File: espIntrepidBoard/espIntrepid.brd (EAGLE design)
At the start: 64 x 56 mm, 23 parts, among them Q1 TRANS_NPN, Q7 TRANS_NPN, U1 ESP32DEV_38, U2 MOSFET_P, U3 LTV-847, U5 SN65HVD232DSOIC8, U6 LTV-817

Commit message: Finished board
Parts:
- moved R1 0.50 mm to (56.0, 47.5)
- moved JP7 0.10 mm to (61.0, 3.40)
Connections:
- net N$7: now also JP1.6; no longer JP1.7
- net N$8: now also JP1.7; no longer JP1.6
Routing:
- net N$8: track 35.6 -> 29.7 mm, vias 2 -> 0
- net N$7: track 28.6 -> 26.4 mm
- net +12V: track 79.1 -> 79.9 mm
- net ABS_UC: track 7.32 -> 6.72 mm
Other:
- outline, holes or cut-outs redrawn
- board text added: "ESP32_Dashboard V 1.0 2/16/25"
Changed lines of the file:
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@@
 <board>
 <plain>
-<wire x1="0" y1="0" x2="64" y2="0" width="0" layer="20"/>
-<wire x1="64" y1="0" x2="64" y2="56" width="0" layer="20"/>
-<wire x1="64" y1="56" x2="0" y2="56" width="0" layer="20"/>
-<wire x1="0" y1="56" x2="0" y2="0" width="0" layer="20"/>
 <hole x="3.5" y="3.5" drill="2.5"/>
 <hole x="3.5" y="52.5" drill="2.5"/>
 <hole x="55" y="3.5" drill="2.5"/>
 <hole x="55" y="52.5" drill="2.5"/>
+<wire x1="3" y1="0" x2="61" y2="0" width="0" layer="20"/>
+<wire x1="64" y1="3" x2="64" y2="53" width="0" layer="20"/>
+<wire x1="61" y1="56" x2="3" y2="56" width="0" layer="20"/>
+<wire x1="0" y1="53" x2="0" y2="3" width="0" layer="20"/>
+<wire x1="0" y1="53" x2="3" y2="56" width="0" layer="20" curve="-90"/>
+<wire x1="61" y1="56" x2="64" y2="53" width="0" layer="20" curve="-90"/>
+<wire x1="64" y1="3" x2="61" y2="0" width="0" layer="20" curve="-90"/>
+<wire x1="3" y1="0" x2="0" y2="3" width="0" layer="20" curve="-90"/>
+<text x="14.5" y="51" size="1.27" layer="25">ESP32_Dashboard
+V 1.0      2/16/25</text>
 </plain>
 <attributes>
@@
 <attribute name="NAME" x="50.2" y="48.6" size="0.6096" layer="25" rot="R270"/>
 </element>
-<element name="R1" library="DR" package="M1206" value="" x="56" y="48" smashed="yes">
-<attribute name="NAME" x="58.73" y="47.27" size="1.27" layer="25"/>
-<attribute name="VALUE" x="54.73" y="45.46" size="1.27" layer="27"/>
+<element name="R1" library="DR" package="M1206" value="" x="56" y="47.5" smashed="yes">
+<attribute name="NAME" x="58.73" y="46.77" size="1.27" layer="25"/>
+<attribute name="VALUE" x="54.73" y="44.96" size="1.27" layer="27"/>
 </element>
 <element name="Q1" library="DR" package="SOT-23" value="TRANS_NPN" x="47" y="47" smashed="yes" rot="R270">
@@
 <attribute name="NAME" x="45.7" y="21.6" size="1.778" layer="25"/>
 </element>
-<element name="JP7" library="pinhead" library_urn="urn:adsk.eagle:library:325" package="1X02" package3d_urn="urn:adsk.eagle:package:22435/2" value="" x="61" y="3.3" smashed="yes" rot="R270">
-<attribute name="NAME" x="62.8288" y="5.9162" size="1.27" layer="25" ratio="10" rot="R270"/>
-<attribute name="POPULARITY" value="98" x="61" y="3.3" size="1.778" layer="27" rot="R270" display="off"/>
-<attribute name="VALUE" x="57.825" y="5.84" size="1.27" layer="27" rot="R270"/>
+<element name="JP7" library="pinhead" library_urn="urn:adsk.eagle:library:325" package="1X02" package3d_urn="urn:adsk.eagle:package:22435/2" value="" x="61" y="3.4" smashed="yes" rot="R270">
+<attribute name="NAME" x="62.8288" y="6.0162" size="1.27" layer="25" ratio="10" rot="R270"/>
+<attribute name="POPULARITY" value="98" x="61" y="3.4" size="1.778" layer="27" rot="R270" display="off"/>
+<attribute name="VALUE" x="57.825" y="5.94" size="1.27" layer="27" rot="R270"/>
 </element>
 </elements>
@@
 <vertex x="39" y="56.5"/>
 <vertex x="65.5" y="56.5"/>
-<vertex x="65.5" y="0"/>
-<vertex x="-0.5" y="0"/>
+<vertex x="65.5" y="-1"/>
+<vertex x="-0.5" y="-1"/>
 </polygon>
 <contactref element="JP2" pad="3"/>
@@
 <vertex x="-0.5" y="41.5"/>
 <vertex x="39" y="41.5"/>
-<vertex x="39" y="56"/>
-<vertex x="64.5" y="56"/>
+<vertex x="39" y="57"/>
+<vertex x="64.5" y="57"/>
 <vertex x="64.5" y="-0.5"/>
 </polygon>
@@
 <contactref element="U3" pad="16"/>
 <contactref element="U3" pad="14"/>
-<wire x1="55" y1="36.92" x2="53" y2="36.92" width="0.508" layer="1"/>
-<wire x1="53" y1="36.92" x2="52.58" y2="36.92" width="0.508" layer="1"/>
-<wire x1="52.58" y1="36.92" x2="51.5" y2="38" width="0.508" layer="1"/>
-<wire x1="51.5" y1="38" x2="51.5" y2="41" width="0.508" layer="1"/>
-<wire x1="51.5" y1="41" x2="52.5" y2="42" width="0.508" layer="1"/>
+<wire x1="55" y1="36.92" x2="53" y2="36.92" width="0.8128" layer="1"/>
+<wire x1="53" y1="36.92" x2="52.58" y2="36.92" width="0.8128" layer="1"/>
+<wire x1="52.58" y1="36.92" x2="51.5" y2="38" width="0.8128" layer="1"/>
+<wire x1="51.5" y1="38" x2="51.5" y2="41" width="0.8128" layer="1"/>
+<wire x1="51.5" y1="41" x2="52.5" y2="42" width="0.8128" layer="1"/>
 <wire x1="52.5" y1="42" x2="55" y2="42" width="0.508" layer="1"/>
-<wire x1="42.46" y1="52.9" x2="42.5" y2="52.86" width="0.508" layer="1"/>
-<wire x1="53.54381875" y1="49.95" x2="53.56381875" y2="49.95" width="0.508" layer="1"/>
-<wire x1="53.56381875" y1="49.95" x2="56" y2="49.95" width="0.508" layer="1"/>
-<wire x1="42.46" y1="52.9" x2="45.38" y2="49.95" width="0.508" layer="1"/>
-<wire x1="45.38" y1="49.95" x2="53.54381875" y2="49.95" width="0.508" layer="1"/>
-<wire x1="56" y1="49.95" x2="57.4" y2="48.6" width="0.508" layer="1"/>
-<wire x1="57.4" y1="48.6" x2="57.4" y2="48" width="0.508" layer="1"/>
-<wire x1="57.4" y1="48" x2="57.4" y2="44.4" width="0.508" layer="1"/>
-<wire x1="57.4" y1="44.4" x2="55" y2="42" width="0.508" layer="1"/>
-<wire x1="55" y1="42" x2="53.45" y2="42" width="0.4064" layer="1"/>
+<wire x1="44.374915625" y1="49.45" x2="42.46" y2="51.3845875" width="0.8128" layer="1"/>
+<wire x1="42.46" y1="52.9" x2="42.46" y2="51.3845875" width="0.8128" layer="1"/>
+<wire x1="44.374915625" y1="49.45" x2="56.51851875" y2="49.45" width="0.8128" layer="1"/>
+<wire x1="56.51851875" y1="49.45" x2="57.4" y2="48.6" width="0.8128" layer="1"/>
+<wire x1="57.4" y1="48.6" x2="57.4" y2="47.5" width="0.508" layer="1"/>
+<wire x1="57.4" y1="47.5" x2="57.4" y2="44.4" width="0.8128" layer="1"/>
+<wire x1="57.4" y1="44.4" x2="55" y2="42" width="0.8128" layer="1"/>
+<wire x1="55" y1="42" x2="53.45" y2="42" width="0.8128" layer="1"/>
 <wire x1="53.45" y1="42" x2="49.4" y2="46.05" width="0.4064" layer="1"/>
 <contactref element="JP7" pad="1"/>
-<wire x1="61" y1="4.57" x2="59.93" y2="4.57" width="0.8128" layer="16"/>
+<wire x1="61" y1="4.67" x2="59.93" y2="4.57" width="0.8128" layer="16"/>
 <wire x1="53.5" y1="11" x2="53.5" y2="36.5" width="0.8128" layer="16"/>
 <wire x1="53.5" y1="36.5" x2="53" y2="36.5" width="0.8128" layer="16"/>
@@
 <wire x1="47.1" y1="47" x2="48.05" y2="47.95" width="0.508" layer="1"/>
 <wire x1="48.05" y1="47.95" x2="49.4" y2="47.95" width="0.508" layer="1"/>
-<wire x1="49.4" y1="47.95" x2="49.95" y2="48.5" width="0.508" layer="1"/>
-<wire x1="49.95" y1="48.5" x2="54.5" y2="48.5" width="0.508" layer="1"/>
-<wire x1="54.5" y1="48.5" x2="54.6" y2="48.4" width="0.508" layer="1"/>
-<wire x1="54.6" y1="48.4" x2="54.6" y2="48" width="0.508" layer="1"/>
+<wire x1="49.4" y1="47.95" x2="49.45" y2="48" width="0.508" layer="1"/>
+<wire x1="49.45" y1="48" x2="54.5" y2="48" width="0.508" layer="1"/>
+<wire x1="54.5" y1="48" x2="54.6" y2="47.9" width="0.508" layer="1"/>
+<wire x1="54.6" y1="47.9" x2="54.6" y2="47.5" width="0.508" layer="1"/>
 </signal>
 <signal name="ABS">
@@
 <signal name="ABS_UC">
 <contactref element="R8" pad="1"/>
-<wire x1="39.68" y1="26.92" x2="40.1" y2="26.5" width="0.4064" layer="1"/>
 <contactref element="U1" pad="30"/>
 <wire x1="34.9" y1="30.18" x2="36.42" y2="30.18" width="0.6096" layer="1"/>
@@
 <signal name="N$7">
 <contactref element="JP1" pad="3"/>
-<contactref element="JP1" pad="7"/>
 <contactref element="U1" pad="15"/>
 <wire x1="9.5" y1="14.94" x2="7.56" y2="14.94" width="0.508" layer="1"/>
@@
 <wire x1="5.34" y1="25.16" x2="3.1" y2="25.16" width="0.508" layer="16"/>
 <wire x1="6" y1="24.5" x2="5.34" y2="25.16" width="0.508" layer="16"/>
-<wire x1="3.1" y1="35.32" x2="5.18" y2="35.32" width="0.508" layer="16"/>
-<wire x1="5.18" y1="35.32" x2="6" y2="34.5" width="0.508" layer="16"/>
-<wire x1="6" y1="34.5" x2="6" y2="24.5" width="0.508" layer="16"/>
+<wire x1="6" y1="32.5" x2="5.68" y2="32.82" width="0.508" layer="16"/>
+<wire x1="6" y1="32.5" x2="6" y2="24.5" width="0.508" layer="16"/>
+<contactref element="JP1" pad="6"/>
+<wire x1="5.68" y1="32.82" x2="3.14" y2="32.82" width="0.4064" layer="16"/>
+<wire x1="3.14" y1="32.82" x2="3.1" y2="32.78" width="0.4064" layer="16"/>
 </signal>
 <signal name="N$8">
-<contactref element="JP1" pad="6"/>
 <contactref element="JP1" pad="2"/>
 <contactref element="U1" pad="12"/>
 <wire x1="9.5" y1="22.56" x2="3.16" y2="22.56" width="0.508" layer="1"/>
 <wire x1="3.16" y1="22.56" x2="3.1" y2="22.62" width="0.508" layer="1"/>
-<wire x1="3.1" y1="32.78" x2="6.78" y2="32.78" width="0.508" layer="1"/>
-<wire x1="6.78" y1="32.78" x2="7" y2="33" width="0.508" layer="1"/>
-<wire x1="7" y1="33" x2="7" y2="36.5" width="0.508" layer="1"/>
-<via x="7" y="36.5" extent="1-16" drill="0.6096"/>
-<via x="11.5" y="36.5" extent="1-16" drill="0.6096"/>
-<wire x1="11.5" y1="36.5" x2="12.5" y2="35.5" width="0.508" layer="1"/>
+<wire x1="11" y1="34" x2="12.5" y2="32.5" width="0.508" layer="1"/>
 <wire x1="12.5" y1="23" x2="12" y2="22.5" width="0.508" layer="1"/>
 <wire x1="12" y1="22.5" x2="9.56" y2="22.5" width="0.508" layer="1"/>
 <wire x1="9.56" y1="22.5" x2="9.5" y2="22.56" width="0.508" layer="1"/>
-<wire x1="7" y1="36.5" x2="11.5" y2="36.5" width="0.254" layer="16"/>
-<wire x1="12.5" y1="35.5" x2="12.5" y2="23" width="0.508" layer="1"/>
+<wire x1="12.5" y1="32.5" x2="12.5" y2="23" width="0.508" layer="1"/>
+<contactref element="JP1" pad="7"/>
+<wire x1="3.1" y1="35.32" x2="6.18" y2="35.32" width="0.4064" layer="1"/>
+<wire x1="6.18" y1="35.32" x2="7.5" y2="34" width="0.4064" layer="1"/>
+<wire x1="7.5" y1="34" x2="11" y2="34" width="0.3048" layer="1"/>
 </signal>
 </signals>
@@
 </drawing>
 <compatibility>
+<note version="6.3" minversion="6.2.2" severity="warning">
+Since Version 6.2.2 text objects can contain more than one line,
+which will not be processed correctly with this version.
+</note>
 <note version="8.2" severity="warning">
 Since Version 8.2, EAGLE supports online libraries. The ids

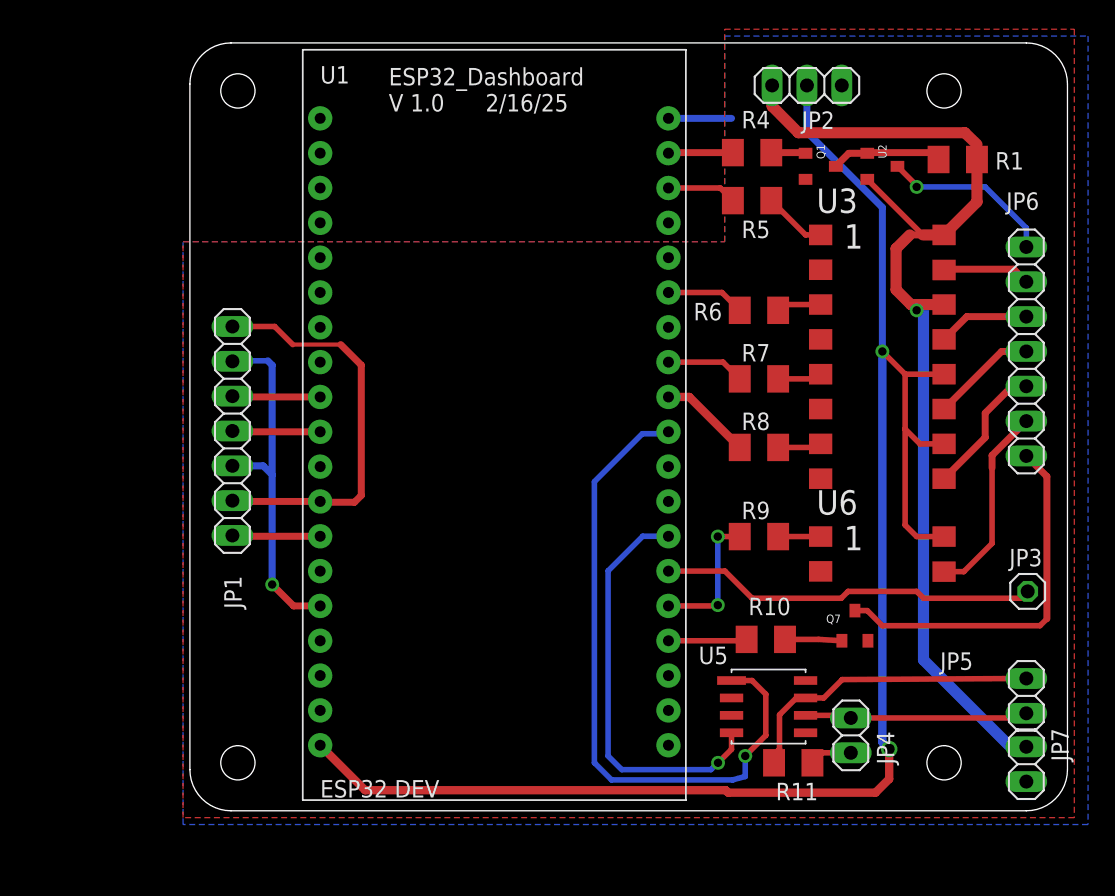
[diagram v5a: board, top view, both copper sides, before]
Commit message: Made fixes to board, started V1.1
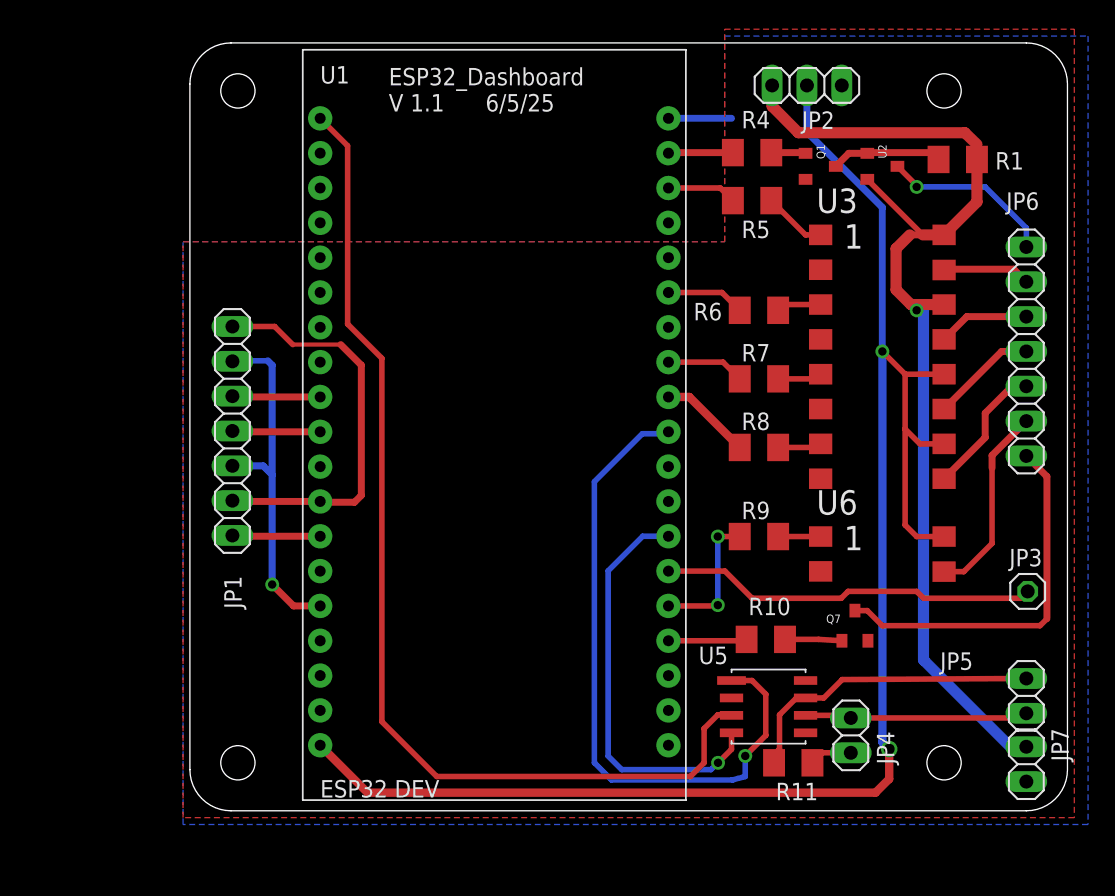
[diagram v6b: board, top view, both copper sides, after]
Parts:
- U5: value SN65HVD232DSOIC8 -> SN65HVD233D
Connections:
- new net 3.3V: U1.1, U5.3
- net GND: now also U5.8
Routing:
- net 3.3V: track 0.00 -> 76.4 mm
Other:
- board text added: "ESP32_Dashboard V 1.1 6/5/25"
- board text removed: "ESP32_Dashboard V 1.0 2/16/25"
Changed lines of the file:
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@@
 <layer number="56" name="wert" color="7" fill="1" visible="no" active="no"/>
 <layer number="57" name="tCAD" color="7" fill="1" visible="no" active="no"/>
+<layer number="88" name="SimResults" color="9" fill="1" visible="no" active="no"/>
+<layer number="89" name="SimProbes" color="9" fill="1" visible="no" active="no"/>
 <layer number="90" name="Modules" color="5" fill="1" visible="no" active="no"/>
 <layer number="91" name="Nets" color="2" fill="1" visible="no" active="no"/>
@@
 <wire x1="3" y1="0" x2="0" y2="3" width="0" layer="20" curve="-90"/>
 <text x="14.5" y="51" size="1.27" layer="25">ESP32_Dashboard
-V 1.0      2/16/25</text>
+V 1.1      6/5/25</text>
 </plain>
 <attributes>
@@
 <attribute name="VALUE" x="40.73" y="9.96" size="1.27" layer="27"/>
 </element>
-<element name="U5" library="DR" package="SOIC-8" value="SN65HVD232DSOIC8" x="39.5" y="9.5" smashed="yes">
+<element name="U5" library="DR" package="SOIC-8" value="SN65HVD233D" x="39.5" y="9.5" smashed="yes">
 <attribute name="NAME" x="37.1" y="10.7" size="1.27" layer="25" ratio="3"/>
 </element>
@@
 <contactref element="U1" pad="32"/>
 <contactref element="JP7" pad="2"/>
+<contactref element="U5" pad="8"/>
 </signal>
 <signal name="+5V">
 <contactref element="JP2" pad="2"/>
 <contactref element="U1" pad="19"/>
-<wire x1="12.78" y1="1.5" x2="9.5" y2="4.78" width="0.6096" layer="1"/>
+<wire x1="12.9592" y1="1.3208" x2="9.5" y2="4.78" width="0.6096" layer="1"/>
 <contactref element="U3" pad="12"/>
 <contactref element="U3" pad="10"/>
@@
 <wire x1="52.16" y1="27.84" x2="52.16" y2="20.84" width="0.4064" layer="1"/>
 <wire x1="52.16" y1="20.84" x2="53" y2="20" width="0.4064" layer="1"/>
-<wire x1="39.07915625" y1="1.5" x2="39.25835625" y2="1.3208" width="0.6096" layer="1"/>
-<wire x1="39.25835625" y1="1.3208" x2="50" y2="1.3208" width="0.6096" layer="1"/>
 <wire x1="51" y1="2.3208" x2="50" y2="1.3208" width="0.6096" layer="1"/>
-<wire x1="12.78" y1="1.5" x2="39.07915625" y2="1.5" width="0.6096" layer="1"/>
+<wire x1="12.9592" y1="1.3208" x2="50" y2="1.3208" width="0.6096" layer="1"/>
 <wire x1="50.5" y1="33.5" x2="50.5" y2="5" width="0.6096" layer="16"/>
 <wire x1="50.5" y1="5" x2="51" y2="4.5" width="0.6096" layer="16"/>
@@
 <wire x1="7.5" y1="34" x2="11" y2="34" width="0.3048" layer="1"/>
 </signal>
+<signal name="3.3V">
+<contactref element="U5" pad="3"/>
+<contactref element="U1" pad="1"/>
+<wire x1="9.5" y1="50.5" x2="11.5" y2="48.5" width="0.4064" layer="1"/>
+<wire x1="11.5" y1="48.5" x2="11.5" y2="35.5" width="0.4064" layer="1"/>
+<wire x1="11.5" y1="35.5" x2="14" y2="33" width="0.4064" layer="1"/>
+<wire x1="14" y1="33" x2="14" y2="6.5" width="0.4064" layer="1"/>
+<wire x1="14" y1="6.5" x2="18" y2="2.5" width="0.4064" layer="1"/>
+<wire x1="18" y1="2.5" x2="36.5" y2="2.5" width="0.4064" layer="1"/>
+<wire x1="36.5" y1="2.5" x2="37.5" y2="3.5" width="0.4064" layer="1"/>
+<wire x1="37.5" y1="3.5" x2="37.5" y2="6" width="0.4064" layer="1"/>
+<wire x1="37.5" y1="6" x2="38.5" y2="7" width="0.4064" layer="1"/>
+<wire x1="38.5" y1="7" x2="39.46" y2="7" width="0.4064" layer="1"/>
+<wire x1="39.46" y1="7" x2="39.5" y2="6.96" width="0.4064" layer="1"/>
+</signal>
 </signals>
